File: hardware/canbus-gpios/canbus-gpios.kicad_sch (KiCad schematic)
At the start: 33 parts, among them J1 USB_B_Micro, J2 UART, J3 10k NTC, J4 CANBus, J5 CANBus, J6 SWD, Q1 2N7002, Q2 2N7002, U1 MCP1754S-3302xCB, U2 STM32F042F6Px, U3 Voltage Regulator, U4 MCP2562HD

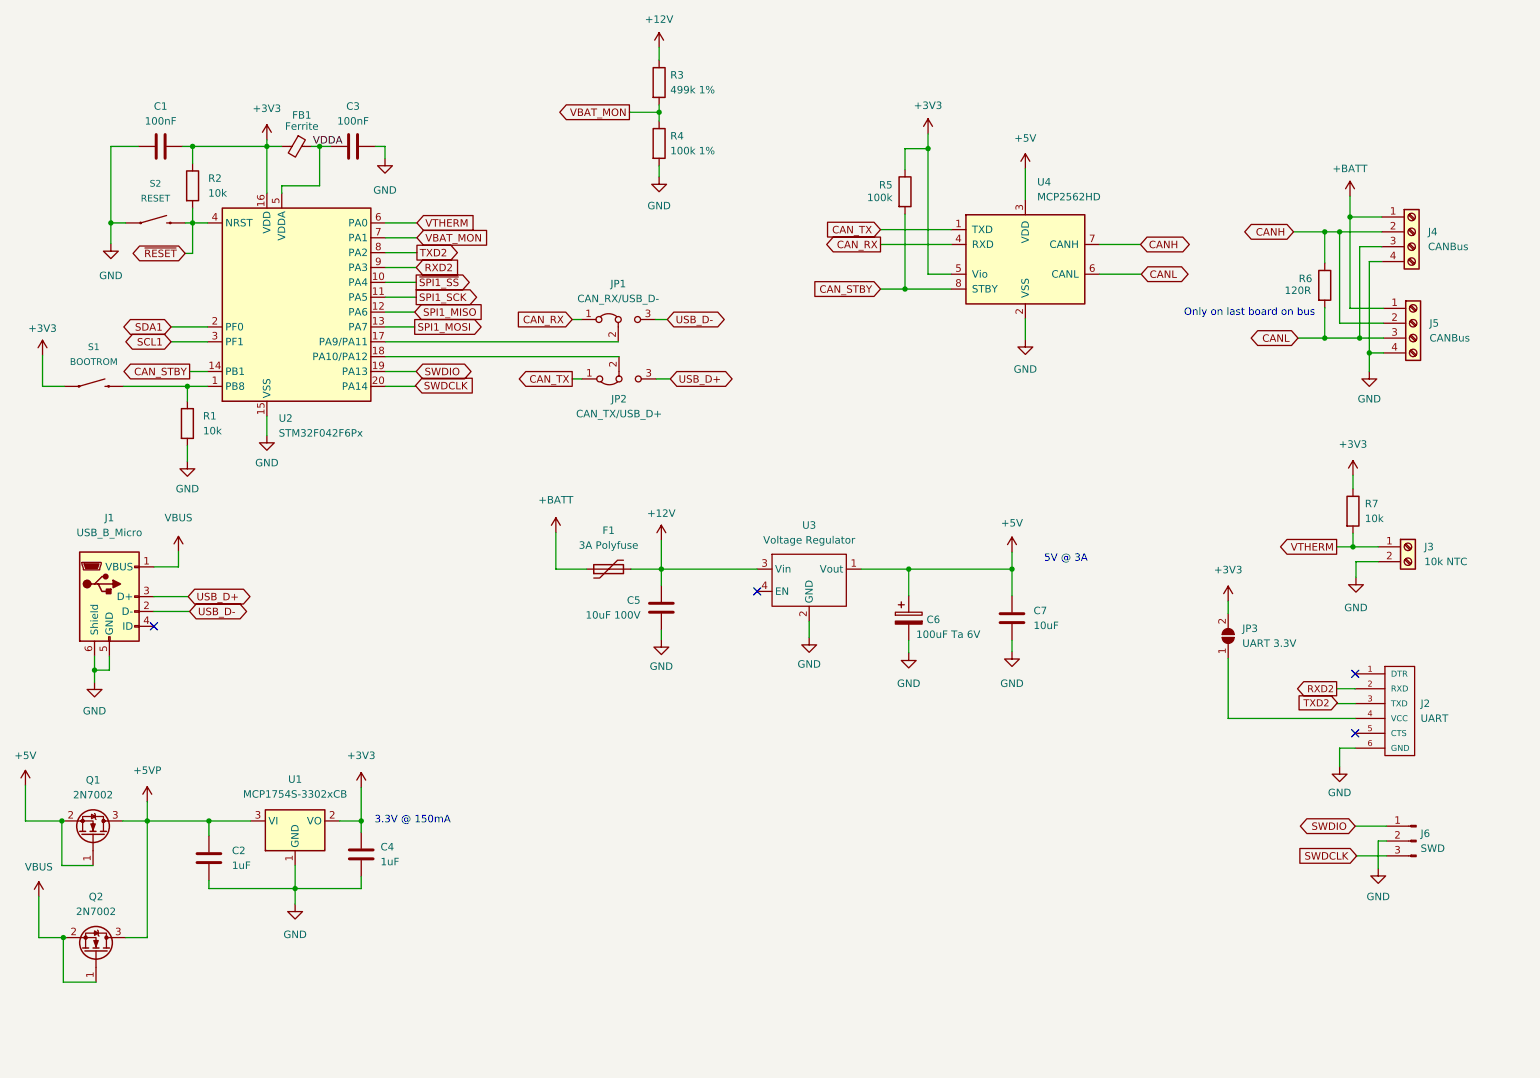
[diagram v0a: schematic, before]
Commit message: Updated canbus-gpios to do GPIOs
- START_RUN and IGNITION_SENSE are active high 12V.
- EMERGENCY_STOP is active low 12V.
- all GPIOs converted to active high 3.3V at the CPU
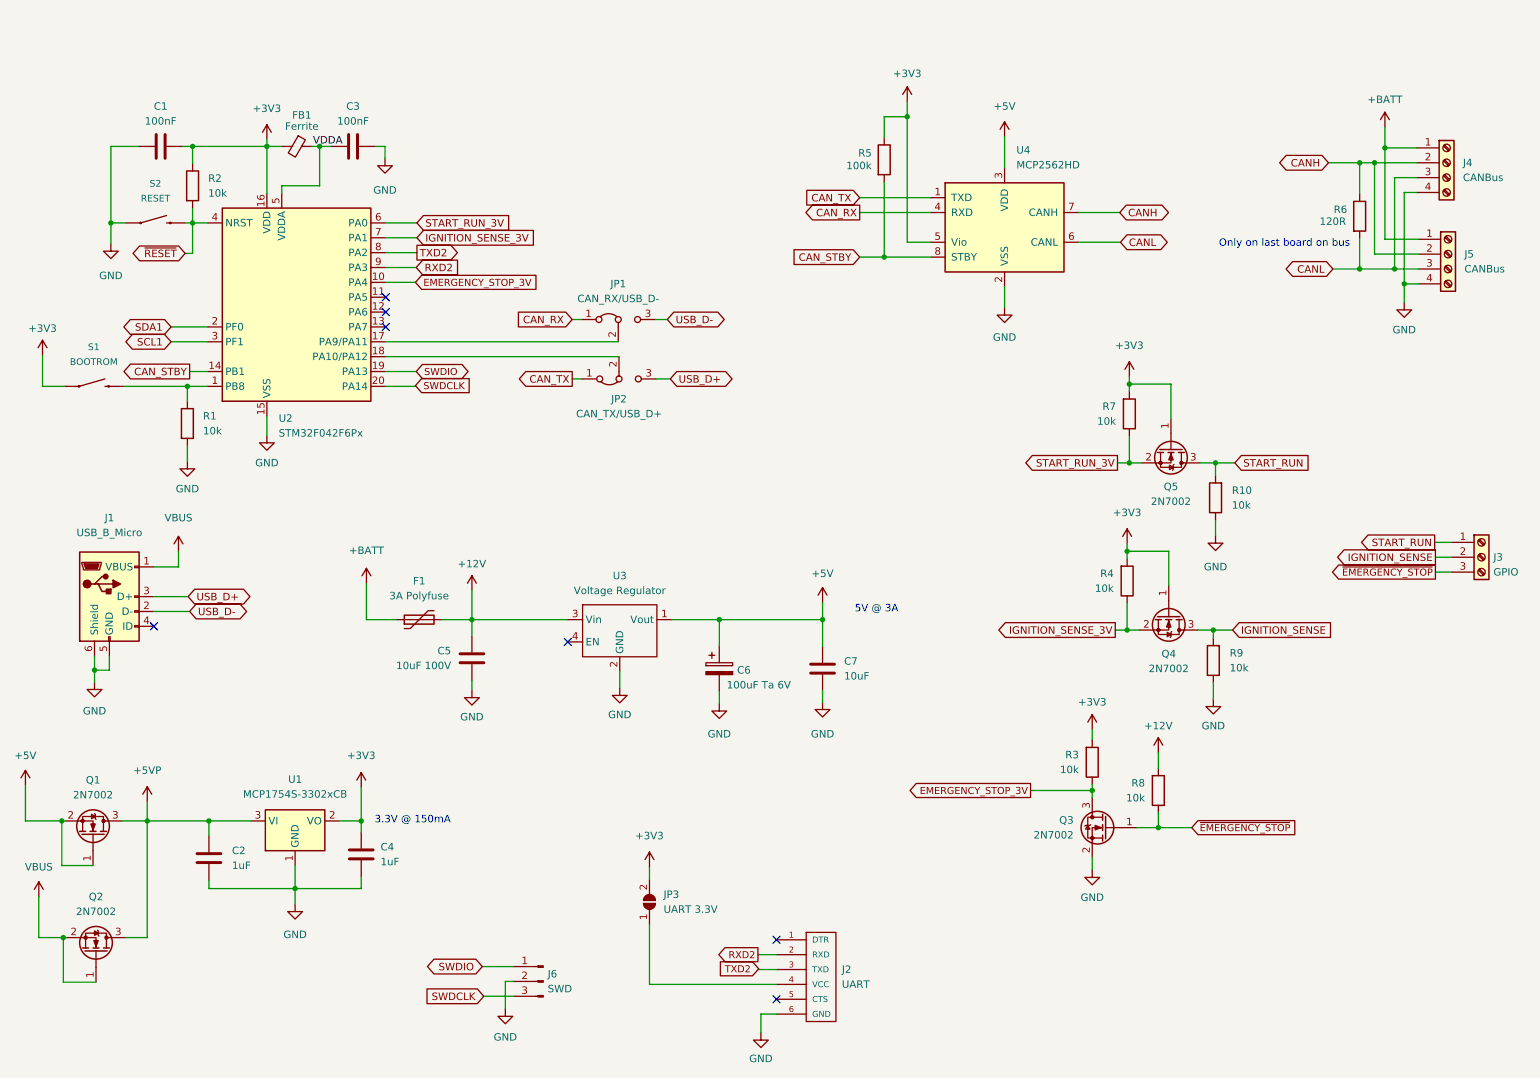
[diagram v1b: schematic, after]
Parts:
- removed J3: 10k NTC, TerminalBlock_TE-Connectivity:TerminalBlock_TE_282834-2_1x02_P2.54mm_Horizontal, symbol Connector:Screw_Terminal_01x02
- added J3: GPIO, TerminalBlock_TE-Connectivity:TerminalBlock_TE_282834-3_1x03_P2.54mm_Horizontal, symbol Connector:Screw_Terminal_01x03
- added Q3, Q4, Q5: 2N7002, Package_TO_SOT_SMD:SOT-23, symbol Transistor_FET:2N7002
- added R10, R8, R9: 10k, Resistor_SMD:R_0805_2012Metric_Pad1.20x1.40mm_HandSolder, symbol Device:R
- JP3: footprint (none) -> Jumper:SolderJumper-2_P1.3mm_Open_TrianglePad1.0x1.5mm
- R3: value 499k 1% -> 10k
- R4: value 100k 1% -> 10k
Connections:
- net +12V: now also R8.2; no longer R3.1
- net +3V3: now also R3.2, R4.2, R7.2, Q4.1 (G), Q5.1 (G); no longer R7.1
- net GND: now also Q3.2 (S), R10.1, R9.1; no longer R4.2
- net SPI1_MISO: no longer names the net of U2.12 (PA6)
- net SPI1_MOSI: no longer names the net of U2.13 (PA7)
- net SPI1_SCK: no longer names the net of U2.11 (PA5)
- net VBAT_MON renamed IGNITION_SENSE_3V
- net IGNITION_SENSE_3V: now also Q4.2 (S); no longer R3.2
- net VTHERM renamed START_RUN_3V
- net START_RUN_3V: now also R7.1, Q5.2 (S); no longer R7.2
- net ~{SPI1_SS} renamed EMERGENCY_STOP_3V
- net EMERGENCY_STOP_3V: now also R3.1, Q3.3 (D)
- new net IGNITION_SENSE: J3.2 (Pin_2), Q4.3 (D), R9.2
- new net START_RUN: J3.1 (Pin_1), Q5.3 (D), R10.2
- new net ~{EMERGENCY_STOP}: J3.3 (Pin_3), Q3.1 (G), R8.1
- no-connect marks 4 -> 7
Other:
- title: CANBus Thermistor Sensor -> CANBus GPIO Sensor
- moved on the sheet: C5, C6, C7, F1, J2, J4, J5, J6, JP3, R5, R6, U3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

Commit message: Updated canbus-ds1820 board, reannotated canbus-gpios
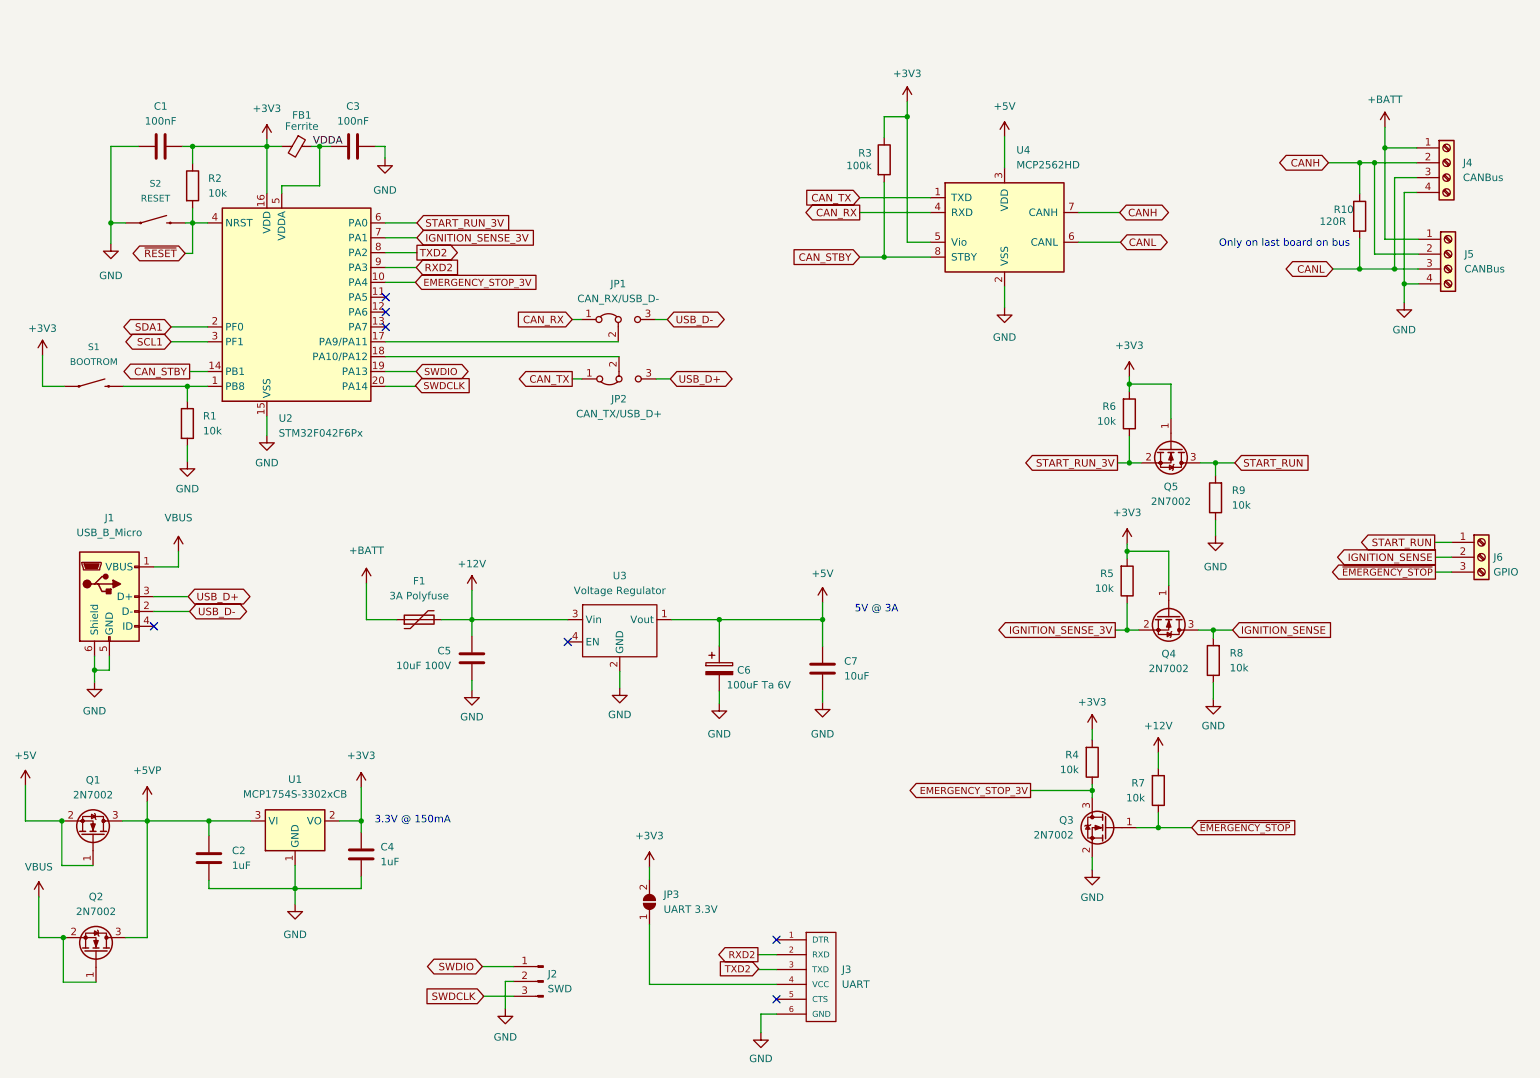
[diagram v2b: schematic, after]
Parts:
- renumbered J6 to J2, J2 to J3, J3 to J6, R6 to R10, R5 to R3, R3 to R4, R4 to R5, R7 to R6, R8 to R7, R9 to R8, R10 to R9
